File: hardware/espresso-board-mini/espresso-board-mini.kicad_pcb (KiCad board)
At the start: 2 copper layers, 50 x 105 mm, 27 parts, among them J5_3V3 J_THERMO_3V3, J5_CS THERMO_CS, J5_GND J_THERMO_GND, J5_SCK THERMO_SCK, J5_SO THERMO_SO, J6_3V3 J_OLED_3V3, J6_GND J_OLED_GND, J6_SCL OLED_SCL, J6_SDA OLED_SDA, U1 ESP32C3_SuperMini

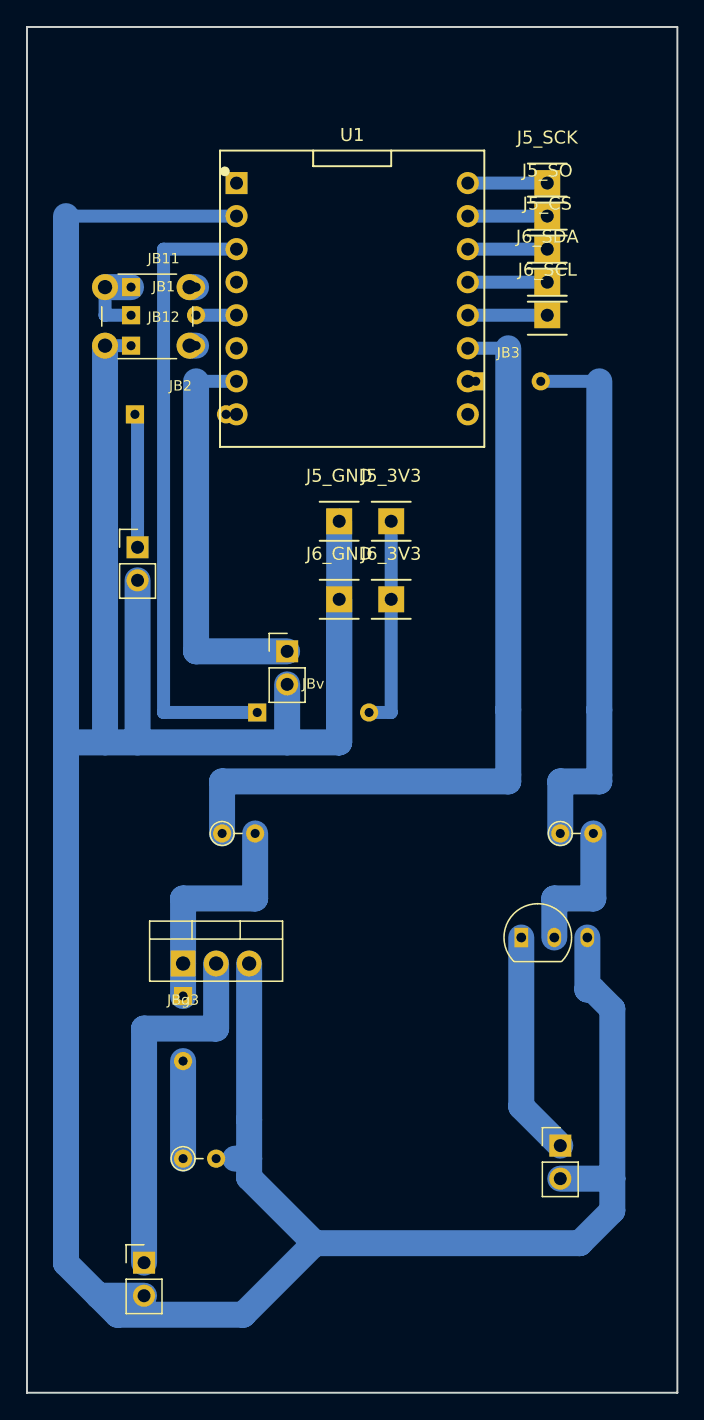
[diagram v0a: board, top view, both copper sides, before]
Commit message: feat(hardware): ajustes de furo e footprints no espresso-board-mini
Co-Authored-By: Claude Sonnet 5 <noreply@anthropic.com>
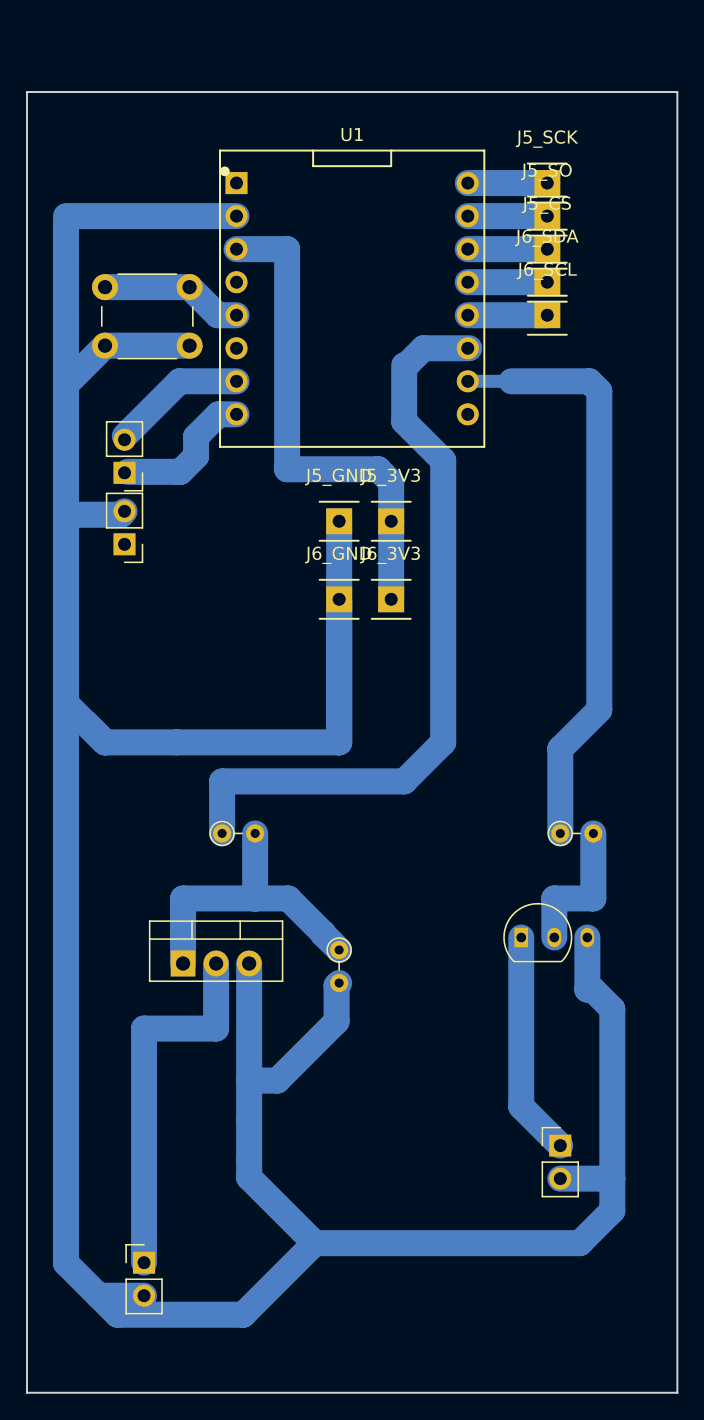
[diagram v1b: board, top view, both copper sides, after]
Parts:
- removed JB1, JB11, JB12, JB2, JB3, JBg3, JBv: , Jumper:SolderBridge_2Pad
- moved ? 20.0 mm to (24.0, 71.0), turned to -90 degrees
- moved ? 15.0 mm to (7.50, 39.8), turned to 180 degrees
- moved ? 5.81 mm to (7.50, 34.3), turned to 180 degrees
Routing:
- net +3V3: track 64.8 -> 38.2 mm
- net READY_GPIO1: track 30.9 -> 10.3 mm
- net SSR_ACT_GPIO10: track 62.4 -> 57.8 mm
- net GND: track 293.7 -> 297.1 mm
- net LED_ACT_GPIO20: track 42.9 -> 45.6 mm
- net Q2_BASE: track 25.5 -> 23.7 mm
- net BTN_GPIO3: track 9.77 -> 11.0 mm
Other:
- board size 50 x 105 mm -> 50 x 100 mm

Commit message: fix(hardware): padroniza furação do espresso-board-mini para 1.1mm
Todos os drills de pad THT ajustados para 1.1mm. Pads do TO-92
(0.75mm) tiveram o size alargado de 1.05x1.5 para 1.4x1.85 para
manter anel de cobre válido com o furo maior.

Co-Authored-By: Claude Sonnet 5 <noreply@anthropic.com>
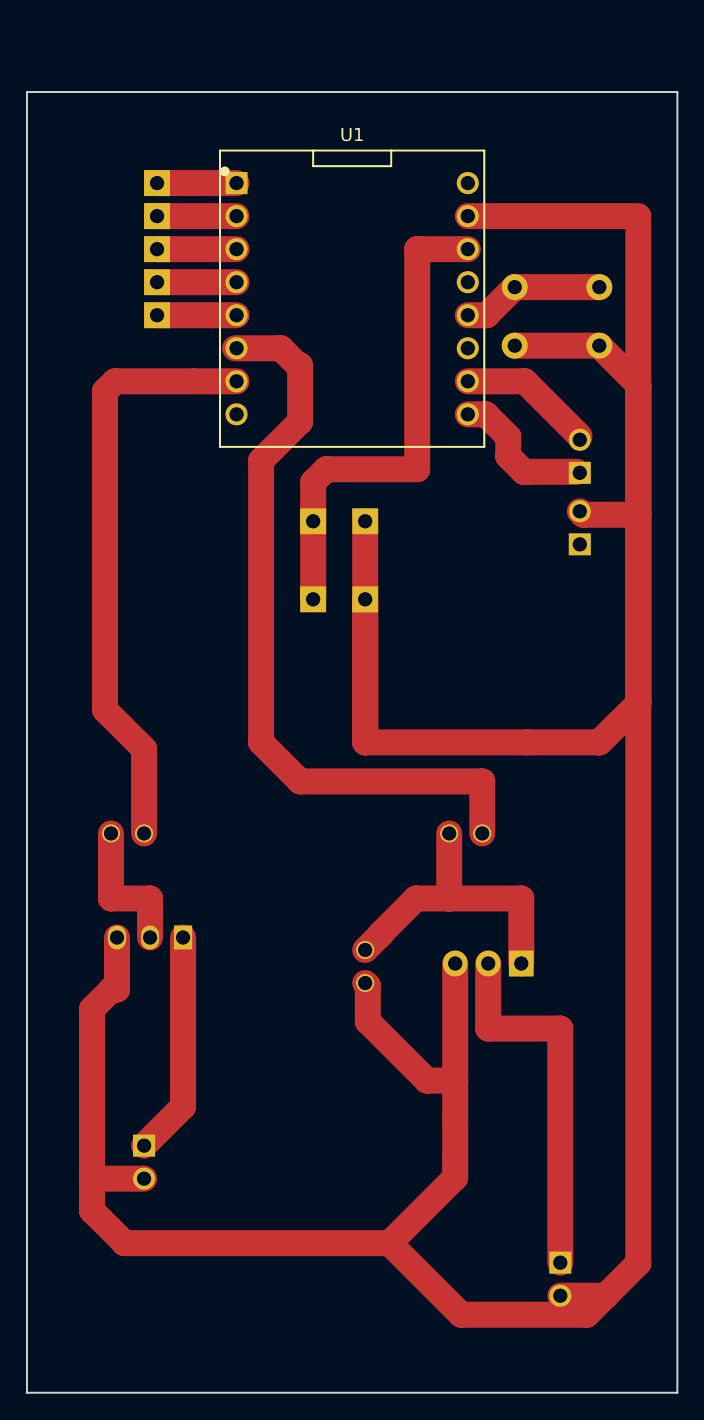
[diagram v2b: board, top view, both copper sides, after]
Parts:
- ? (x10), J5_3V3, J5_CS, J5_GND, J5_SCK, J5_SO, J6_3V3, J6_GND, J6_SCL, J6_SDA: moved to B.Cu
- moved ? 38.0 mm to (44.0, 20.0), turned to 180 degrees
- moved ? 35.0 mm to (42.5, 34.3), turned to 0 degrees
- moved ? 35.0 mm to (42.5, 39.8), turned to 0 degrees
- moved ? 32.0 mm to (9.00, 86.0), turned to 180 degrees
- moved ? 32.0 mm to (41.0, 95.0), turned to 180 degrees
- moved ? 32.0 mm to (9.00, 62.0), turned to 180 degrees
- moved J5_CS 30.0 mm to (10.0, 17.1), turned to 180 degrees
- moved J5_SCK 30.0 mm to (10.0, 12.0), turned to 180 degrees
- moved J5_SO 30.0 mm to (10.0, 14.5), turned to 180 degrees
- moved J6_SCL 30.0 mm to (10.0, 22.2), turned to 180 degrees
- moved J6_SDA 30.0 mm to (10.0, 19.6), turned to 180 degrees
- moved ? 26.0 mm to (38.0, 72.0), turned to 180 degrees
- moved ? 26.0 mm to (12.0, 70.0), turned to 180 degrees
- moved ? 20.0 mm to (35.0, 62.0), turned to 180 degrees
- moved J5_3V3 6.00 mm to (22.0, 38.0), turned to 180 degrees
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
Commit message: fix(hardware): atualiza roteamento e reexporta STEP do espresso-board-mini
Adiciona .gitignore para lockfiles KiCad (*.lck).

Co-Authored-By: Claude Sonnet 5 <noreply@anthropic.com>
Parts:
- moved ? 10.0 mm to (41.0, 85.0)
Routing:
- net GND: track 297.1 -> 274.1 mm
- net SSR_MINUS: track 28.5 -> 18.5 mm
- net +3V3: track 38.2 -> 36.8 mm
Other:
- board size 50 x 100 mm -> 50 x 91.5 mm
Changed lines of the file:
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@@
 		(capping no)
 		(filling no)
-		(zone_defaults)
 		(pcbplotparams
 			(layerselection 0x00000000_00000000_55555555_5755f5ff)
@@
 	(footprint "Connector_PinHeader_2.54mm:PinHeader_1x02_P2.54mm_Vertical"
 		(layer "B.Cu")
-		(at 41 95 180)
+		(at 41 85 180)
 		(descr "Through hole straight pin header, 1x02, 2.54mm pitch, single row")
 		(tags "Through hole pin header THT 1x02 2.54mm single row")
@@
 	(gr_rect
 		(start 0 5)
-		(end 50 105)
+		(end 50 96.5)
 		(stroke
 			(width 0.15)
@@
 	)
 	(segment
-		(start 27.22 69.69)
-		(end 27.22 69.74)
-		(width 2)
-		(layer "F.Cu")
-		(net "Q2_BASE")
-	)
-	(segment
-		(start 29.91 67)
-		(end 27.22 69.69)
-		(width 2)
-		(layer "F.Cu")
-		(net "Q2_BASE")
-	)
-	(segment
-		(start 32.46 67)
-		(end 38 67)
-		(width 2)
-		(layer "F.Cu")
-		(net "Q2_BASE")
-	)
-	(segment
-		(start 38 67)
-		(end 38 72)
-		(width 2)
-		(layer "F.Cu")
-		(net "Q2_BASE")
-	)
-	(segment
-		(start 32.46 67)
-		(end 29.91 67)
-		(width 2)
-		(layer "F.Cu")
-		(net "Q2_BASE")
-	)
-	(segment
-		(start 27.22 69.74)
-		(end 26 70.96)
-		(width 2)
-		(layer "F.Cu")
-		(net "Q2_BASE")
-	)
-	(segment
-		(start 32.46 62)
-		(end 32.46 67)
-		(width 2)
-		(layer "F.Cu")
-		(net "Q2_BASE")
-	)
-	(segment
-		(start 35.46 72)
-		(end 35.46 77)
-		(width 2)
-		(layer "F.Cu")
-		(net "SSR_MINUS")
-	)
-	(segment
-		(start 35.46 77)
-		(end 41 77)
+		(start 6.5 74)
+		(end 6.92 74)
 		(width 2)
 		(layer "F.Cu")
-		(net "SSR_MINUS")
+		(net "GND")
 	)
 	(segment
-		(start 41 77)
-		(end 41 95)
+		(start 26 38)
+		(end 26 49.35753)
 		(width 2)
 		(layer "F.Cu")
-		(net "SSR_MINUS")
+		(net "GND")
 	)
 	(segment
-		(start 6.5 74)
-		(end 6.92 74)
+		(start 26.2 73.7)
+		(end 26 73.5)
 		(width 2)
 		(layer "F.Cu")
@@
 	)
 	(segment
-		(start 47 37.5)
-		(end 47 52)
+		(start 5 88.54)
+		(end 5 75.5)
 		(width 2)
 		(layer "F.Cu")
@@
 	)
 	(segment
-		(start 47 95.04)
-		(end 44.5 97.54)
+		(start 46 15)
+		(end 45.96 15)
 		(width 2)
 		(layer "F.Cu")
@@
 	(segment
 		(start 27.88 93.5)
-		(end 33.38 99)
+		(end 7.5 93.5)
 		(width 2)
 		(layer "F.Cu")
@@
 	)
 	(segment
-		(start 33.89 14.54)
-		(end 47 14.54)
+		(start 43.5 90.5)
+		(end 47 87)
 		(width 2)
 		(layer "F.Cu")
@@
 	)
 	(segment
-		(start 44 55)
-		(end 38.5 55)
+		(start 47 87)
+		(end 47 16)
 		(width 2)
 		(layer "F.Cu")
@@
 	)
 	(segment
-		(start 26 38)
-		(end 26 55)
+		(start 27.88 93.5)
+		(end 40.5 93.5)
 		(width 2)
 		(layer "F.Cu")
@@
 	)
 	(segment
-		(start 26.2 73.7)
-		(end 26 73.5)
+		(start 32.92 84)
+		(end 32.92 87)
 		(width 2)
 		(layer "F.Cu")
@@
 	)
 	(segment
-		(start 5 88.54)
-		(end 5 75.5)
+		(start 47 16)
+		(end 46 15)
 		(width 2)
 		(layer "F.Cu")
@@
 	)
 	(segment
-		(start 43.04 99)
-		(end 44.5 97.54)
+		(start 26 49.35753)
+		(end 26.571235 49.928765)
 		(width 2)
 		(layer "F.Cu")
@@
 	)
 	(segment
-		(start 27.88 93.5)
-		(end 7.5 93.5)
+		(start 41 87.5)
+		(end 41 88)
 		(width 2)
 		(layer "F.Cu")
@@
 	)
 	(segment
-		(start 47 15)
-		(end 47 95.04)
+		(start 42.765 37.5)
+		(end 42.5 37.235)
 		(width 2)
 		(layer "F.Cu")
@@
 	)
 	(segment
-		(start 32.92 84)
-		(end 32.92 87)
+		(start 5 91)
+		(end 7.5 93.5)
 		(width 2)
 		(layer "F.Cu")
@@
 	)
 	(segment
-		(start 38.5 55)
-		(end 26 55)
+		(start 45.5 14.54)
+		(end 33.89 14.54)
 		(width 2)
 		(layer "F.Cu")
@@
 	)
 	(segment
-		(start 47 52)
-		(end 44 55)
+		(start 26.2 76.45)
+		(end 26.2 73.7)
 		(width 2)
 		(layer "F.Cu")
@@
 	)
 	(segment
-		(start 42.765 37.5)
-		(end 42.5 37.235)
+		(start 32.92 72)
+		(end 32.92 81)
 		(width 2)
 		(layer "F.Cu")
@@
 	)
 	(segment
-		(start 41 97.54)
-		(end 44.5 97.54)
+		(start 32.92 81)
+		(end 32.92 84)
 		(width 2)
 		(layer "F.Cu")
@@
 	)
 	(segment
-		(start 5 91)
-		(end 7.5 93.5)
+		(start 28.142469 51.5)
+		(end 43.5 51.5)
 		(width 2)
 		(layer "F.Cu")
@@
 	)
 	(segment
-		(start 45.5 53.5)
-		(end 44 55)
+		(start 47 37.5)
+		(end 42.765 37.5)
 		(width 2)
 		(layer "F.Cu")
@@
 	)
 	(segment
-		(start 26.2 76.45)
-		(end 26.2 73.7)
+		(start 44 24.5)
+		(end 37.5 24.5)
 		(width 2)
 		(layer "F.Cu")
@@
 	)
 	(segment
-		(start 33.38 99)
-		(end 43.04 99)
+		(start 30.75 81)
+		(end 26.2 76.45)
 		(width 2)
 		(layer "F.Cu")
@@
 	)
 	(segment
-		(start 32.92 72)
-		(end 32.92 81)
+		(start 26 44)
+		(end 26 49.357531)
 		(width 2)
 		(layer "F.Cu")
@@
 	)
 	(segment
-		(start 32.92 81)
-		(end 32.92 84)
+		(start 43.5 51.5)
+		(end 47 48)
 		(width 2)
 		(layer "F.Cu")
@@
 	)
 	(segment
-		(start 47 37.5)
-		(end 42.765 37.5)
+		(start 6.92 70)
+		(end 6.92 74)
 		(width 2)
 		(layer "F.Cu")
@@
 	)
 	(segment
-		(start 26 44)
-		(end 26 55)
+		(start 47 48)
+		(end 47 37.5)
 		(width 2)
 		(layer "F.Cu")
@@
 	)
 	(segment
-		(start 44 24.5)
-		(end 37.5 24.5)
+		(start 41 88)
+		(end 43.5 90.5)
 		(width 2)
 		(layer "F.Cu")
@@
 	)
 	(segment
-		(start 30.75 81)
-		(end 26.2 76.45)
+		(start 32.92 87)
+		(end 32.92 88.46)
 		(width 2)
 		(layer "F.Cu")
@@
 	)
 	(segment
-		(start 6.92 70)
-		(end 6.92 74)
+		(start 26 49.357531)
+		(end 28.142469 51.5)
 		(width 2)
 		(layer "F.Cu")
@@
 	)
 	(segment
-		(start 32.92 87)
-		(end 32.92 88.46)
+		(start 40.5 93.5)
+		(end 44.682913 89.317086)
 		(width 2)
 		(layer "F.Cu")
@@
 	)
 	(segment
-		(start 30 17.08)
-		(end 30 34)
+		(start 45.96 15)
+		(end 45.5 14.54)
 		(width 2)
 		(layer "F.Cu")
-		(net "+3V3")
+		(net "GND")
 	)
 	(segment
@@
 	)
 	(segment
-		(start 30 34)
+		(start 30 17.08)
+		(end 30 31.5)
+		(width 2)
+		(layer "F.Cu")
+		(net "+3V3")
+	)
+	(segment
+		(start 33.89 17.08)
+		(end 30 17.08)
+		(width 2)
+		(layer "F.Cu")
+		(net "+3V3")
+	)
+	(segment
+		(start 27.5 34)
 		(end 23 34)
 		(width 2)
@@
 	)
 	(segment
-		(start 33.89 17.08)
-		(end 30 17.08)
+		(start 23 34)
+		(end 22 35)
 		(width 2)
 		(layer "F.Cu")
@@
 	)
 	(segment
-		(start 23 34)
-		(end 22 35)
+		(start 30 31.5)
+		(end 27.5 34)
 		(width 2)
 		(layer "F.Cu")
@@
 	)
 	(segment
+		(start 27.22 69.69)
+		(end 27.22 69.74)
+		(width 2)
+		(layer "F.Cu")
+		(net "Q2_BASE")
+	)
+	(segment
+		(start 29.91 67)
+		(end 27.22 69.69)
+		(width 2)
+		(layer "F.Cu")
+		(net "Q2_BASE")
+	)
+	(segment
+		(start 32.46 67)
+		(end 38 67)
+		(width 2)
+		(layer "F.Cu")
+		(net "Q2_BASE")
+	)
+	(segment
+		(start 38 67)
+		(end 38 72)
+		(width 2)
+		(layer "F.Cu")
+		(net "Q2_BASE")
+	)
+	(segment
+		(start 32.46 67)
+		(end 29.91 67)
+		(width 2)
+		(layer "F.Cu")
+		(net "Q2_BASE")
+	)
+	(segment
+		(start 27.22 69.74)
+		(end 26 70.96)
+		(width 2)
+		(layer "F.Cu")
+		(net "Q2_BASE")
+	)
+	(segment
+		(start 32.46 62)
+		(end 32.46 67)
+		(width 2)
+		(layer "F.Cu")
+		(net "Q2_BASE")
+	)
+	(segment
+		(start 35.46 72)
+		(end 35.46 77)
+		(width 2)
+		(layer "F.Cu")
+		(net "SSR_MINUS")
+	)
+	(segment
+		(start 35.46 77)
+		(end 41 77)
+		(width 2)
+		(layer "F.Cu")
+		(net "SSR_MINUS")
+	)
+	(segment
+		(start 41 77)
+		(end 41 85)
+		(width 2)
+		(layer "F.Cu")
+		(net "SSR_MINUS")
+	)
+	(segment
